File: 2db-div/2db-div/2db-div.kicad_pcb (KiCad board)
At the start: 2 copper layers, 63.5 x 43.2 mm, 26 parts, among them J1001 Conn_01x02, J1002 From R2, J1003 Conn_01x02, U1001 MC1458

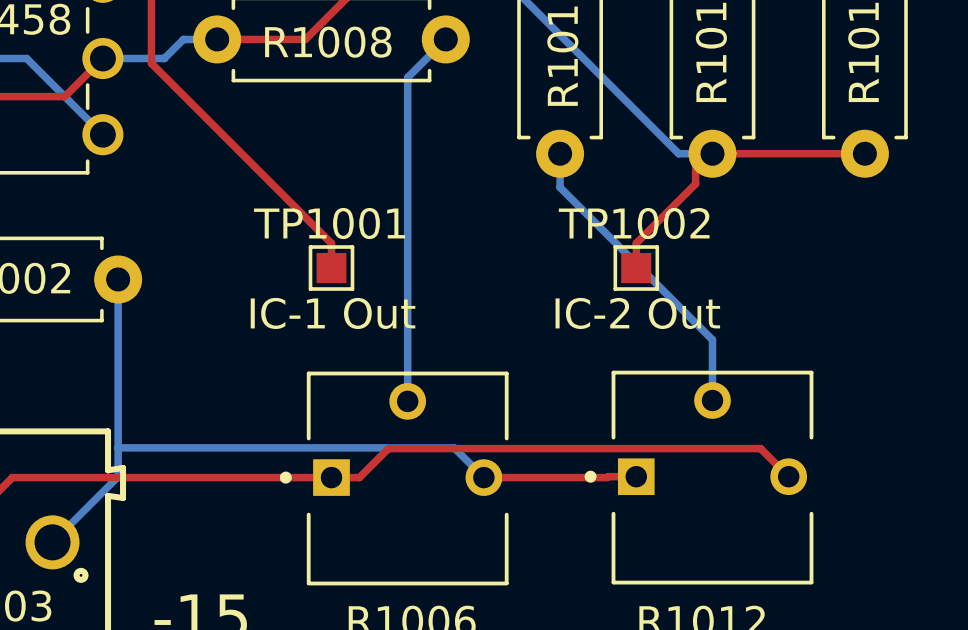
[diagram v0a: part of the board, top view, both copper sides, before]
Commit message: BOM for 2db-div
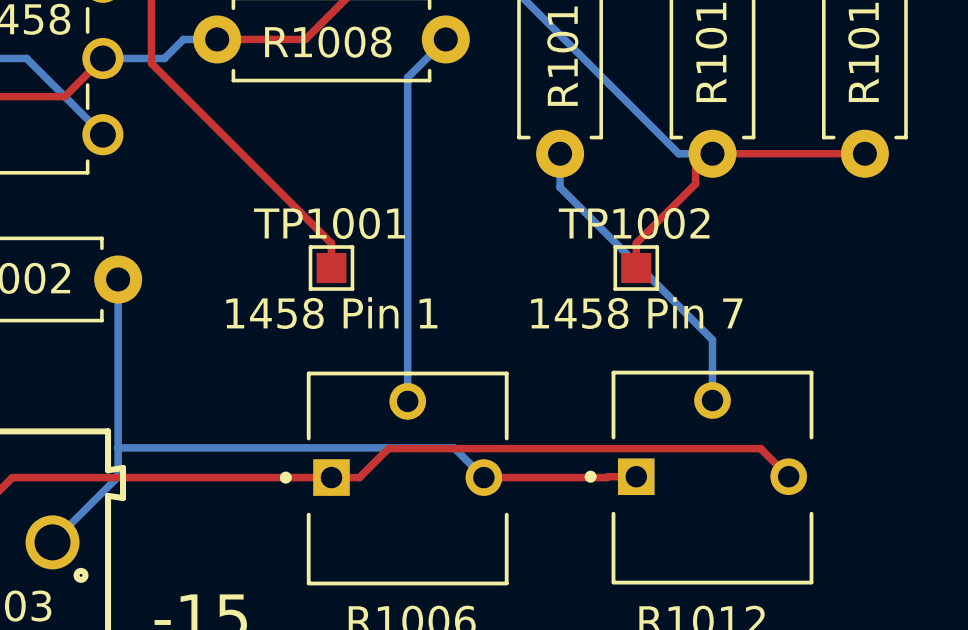
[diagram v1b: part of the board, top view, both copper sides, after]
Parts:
- D1001: value 1N4152 -> 1N4148
- TP1001: value IC-1 Out -> 1458 Pin 1
- TP1002: value IC-2 Out -> 1458 Pin 7
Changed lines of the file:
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@@
       (effects (font (size 1 1) (thickness 0.15)))
     )
-    (fp_text value "IC-2 Out" (at 0 1.55) (layer "F.SilkS")
+    (fp_text value "1458 Pin 7" (at 0 1.55) (layer "F.SilkS")
       (effects (font (size 1 1) (thickness 0.15)))
     )
@@
       (effects (font (size 0.75 0.75) (thickness 0.15)))
     )
-    (fp_text value "1N4152" (at 3.81 2.12) (layer "F.Fab")
+    (fp_text value "1N4148" (at 3.81 2.12) (layer "F.Fab")
       (effects (font (size 1 1) (thickness 0.15)))
     )
@@
       (effects (font (size 1 1) (thickness 0.15)))
     )
-    (fp_text value "IC-1 Out" (at 0 1.55) (layer "F.SilkS")
-      (effects (font (size 1 1) (thickness 0.15)))
-    )
+    (fp_text value "1458 Pin 1" (at 0 1.55) (layer "F.SilkS")
+      (effects (font (size 1 1) (thickness 0.15)))
+    )

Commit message: vco-1stmixer bom
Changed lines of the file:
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@@
   )
   (setup
+    (stackup
+      (layer "F.SilkS" (type "Top Silk Screen"))
+      (layer "F.Paste" (type "Top Solder Paste"))
+      (layer "F.Mask" (type "Top Solder Mask") (thickness 0.01))
+      (layer "F.Cu" (type "copper") (thickness 0.035))
+      (layer "dielectric 1" (type "core") (thickness 1.51) (material "FR4") (epsilon_r 4.5) (loss_tangent 0.02))
+      (layer "B.Cu" (type "copper") (thickness 0.035))
+      (layer "B.Mask" (type "Bottom Solder Mask") (thickness 0.01))
+      (layer "B.Paste" (type "Bottom Solder Paste"))
+      (layer "B.SilkS" (type "Bottom Silk Screen"))
+      (copper_finish "None")
+      (dielectric_constraints no)
+    )
     (pad_to_mask_clearance 0)
     (grid_origin 142.24 139.7)
@@
     (property "Spice_Primitive" "D")
     (attr through_hole)
-    (fp_text reference "D1001" (at 4.191 0) (layer "F.SilkS")
-      (effects (font (size 0.75 0.75) (thickness 0.15)))
+    (fp_text reference "D1001" (at 4.318 0) (layer "F.SilkS")
+      (effects (font (size 0.5 0.5) (thickness 0.125)))
     )
     (fp_text value "1N4148" (at 3.81 2.12) (layer "F.Fab")
@@
       (effects (font (size 1 1) (thickness 0.15)))
     )
-    (fp_text user "*" (at -7.62 -9.0678) (layer "F.SilkS")
-      (effects (font (size 1 1) (thickness 0.15)))
-    )
-    (fp_text user "*" (at -7.62 -9.0678) (layer "F.SilkS")
-      (effects (font (size 1 1) (thickness 0.15)))
-    )
+    (fp_text user "*" (at -8.636 -9.398) (layer "F.SilkS")
+      (effects (font (size 1 1) (thickness 0.15)))
+    )
+    (fp_text user "*" (at -7.874 -9.398) (layer "F.SilkS")
+      (effects (font (size 1 1) (thickness 0.15)))
+    )

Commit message: Minor updates to 2nd db board
primarily renaming nets
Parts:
- H1001, H1002, H1003, H1004: value MountingHole -> type="R" model="MountingHole" lib=""

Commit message: updates to 2db board
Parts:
- added SW1001: 2dB, Connector_Wire:SolderWire-0.5sqmm_1x02_P4.6mm_D0.9mm_OD2.1mm, F.Cu at (197.8, 121.6)
- added SW1002: type="R" model="Video" lib="", Connector_Wire:SolderWire-0.5sqmm_1x02_P4.6mm_D0.9mm_OD2.1mm, F.Cu at (197.8, 125.7)
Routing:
- net Net-(SW1001-A): track 0.00 -> 14.9 mm
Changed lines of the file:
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@@
   (net 12 "Net-(R1009-Pad2)")
   (net 13 "Net-(R1010-Pad2)")
-  (net 14 "Net-(R1013-Pad2)")
+  (net 14 "Net-(SW1001-A)")
+  (net 15 "/Out")
+  (net 16 "Net-(SW1002-Pad1)")
+  (net 17 "unconnected-(SW1002-Pad2)")
   (footprint "MountingHole:MountingHole_3.2mm_M3" (layer "F.Cu")
     (at 199.771 101.6)
@@
     (pad "" np_thru_hole circle (at 0 0) (size 3.2 3.2) (drill 3.2) (layers "*.Cu" "*.Mask"))
   )
+  (footprint "Connector_Wire:SolderWire-0.5sqmm_1x02_P4.6mm_D0.9mm_OD2.1mm" (layer "F.Cu")
+    (at 197.838 121.58)
+    (descr "Soldered wire connection, for 2 times 0.5 mm² wires, basic insulation, conductor diameter 0.9mm, outer diameter 2.1mm, size source Multi-Contact FLEXI-E 0.5 (https://ec.staubli.com/AcroFiles/Catalogues/TM_Cab-Main-11014119_(en)_hi.pdf), bend radius 3 times outer diameter, generated with kicad-footprint-generator")
+    (tags "connector wire 0.5sqmm")
+    (property "Sheetfile" "2db-div.kicad_sch")
+    (property "Sheetname" "")
+    (property "Sim.Device" "SPICE")
+    (property "Sim.Enable" "0")
+    (property "Sim.Params" "type=\"R\" model=\"2dB\" lib=\"\"")
+    (property "Sim.Pins" "1=1 2=2 3=3")
+    (property "ki_description" "Switch, single pole double throw")
+    (property "ki_keywords" "switch single-pole double-throw spdt ON-ON")
+    (attr exclude_from_pos_files)
+    (fp_text reference "SW1001" (at 2.3 -2.25) (layer "F.SilkS")
+        (effects (font (size 1 1) (thickness 0.15)))
+    )
+    (fp_text value "2dB" (at 2.3 2.25) (layer "F.Fab")
+        (effects (font (size 1 1) (thickness 0.15)))
+    )
+    (fp_text user "${REFERENCE}" (at 2.3 0 90) (layer "F.Fab")
+        (effects (font (size 0.78 0.78) (thickness 0.12)))
+    )
+    (fp_line (start -1.8 -1.55) (end -1.8 1.55)
+      (stroke (width 0.05) (type solid)) (layer "F.CrtYd"))
+    (fp_line (start -1.8 1.55) (end 1.8 1.55)
+      (stroke (width 0.05) (type solid)) (layer "F.CrtYd"))
+    (fp_line (start 1.8 -1.55) (end -1.8 -1.55)
+      (stroke (width 0.05) (type solid)) (layer "F.CrtYd"))
+    (fp_line (start 1.8 1.55) (end 1.8 -1.55)
+      (stroke (width 0.05) (type solid)) (layer "F.CrtYd"))
+    (fp_line (start 2.8 -1.55) (end 2.8 1.55)
+      (stroke (width 0.05) (type solid)) (layer "F.CrtYd"))
+    (fp_line (start 2.8 1.55) (end 6.4 1.55)
+      (stroke (width 0.05) (type solid)) (layer "F.CrtYd"))
+    (fp_line (start 6.4 -1.55) (end 2.8 -1.55)
+      (stroke (width 0.05) (type solid)) (layer "F.CrtYd"))
+    (fp_line (start 6.4 1.55) (end 6.4 -1.55)
+      (stroke (width 0.05) (type solid)) (layer "F.CrtYd"))
+    (fp_circle (center 0 0) (end 1.05 0)
+      (stroke (width 0.1) (type solid)) (fill none) (layer "F.Fab"))
+    (fp_circle (center 4.6 0) (end 5.65 0)
+      (stroke (width 0.1) (type solid)) (fill none) (layer "F.Fab"))
+    (pad "1" thru_hole roundrect (at 0 0) (size 2.1 2.1) (drill 1.1) (layers "*.Cu" "*.Mask") (roundrect_rratio 0.119048)
+      (net 14 "Net-(SW1001-A)") (pinfunction "A") (pintype "passive"))
+    (pad "2" thru_hole circle (at 4.6 0) (size 2.1 2.1) (drill 1.1) (layers "*.Cu" "*.Mask")
+      (net 15 "/Out") (pinfunction "B") (pintype "passive"))
+    (model "${KICAD6_3DMODEL_DIR}/Connector_Wire.3dshapes/SolderWire-0.5sqmm_1x02_P4.6mm_D0.9mm_OD2.1mm.wrl"
+      (offset (xyz 0 0 0))
+      (scale (xyz 1 1 1))
+      (rotate (xyz 0 0 0))
+    )
+  )
   (footprint "Resistor_THT:R_Axial_DIN0207_L6.3mm_D2.5mm_P7.62mm_Horizontal" (layer "F.Cu")
     (at 181.61 111.379 180)
@@
     (pad "1" smd rect (at 0 0) (size 1 1) (layers "F.Cu" "F.Mask")
       (net 4 "Net-(D1001-K)") (pinfunction "1") (pintype "passive"))
+  )
+  (footprint "Connector_Wire:SolderWire-0.5sqmm_1x02_P4.6mm_D0.9mm_OD2.1mm" (layer "F.Cu")
+    (at 197.838 125.73)
+    (descr "Soldered wire connection, for 2 times 0.5 mm² wires, basic insulation, conductor diameter 0.9mm, outer diameter 2.1mm, size source Multi-Contact FLEXI-E 0.5 (https://ec.staubli.com/AcroFiles/Catalogues/TM_Cab-Main-11014119_(en)_hi.pdf), bend radius 3 times outer diameter, generated with kicad-footprint-generator")
+    (tags "connector wire 0.5sqmm")
+    (property "Sheetfile" "2db-div.kicad_sch")
+    (property "Sheetname" "")
+    (property "Sim.Device" "SPICE")
+    (property "Sim.Enable" "0")
+    (property "Sim.Params" "type=\"R\" model=\"Video\" lib=\"\"")
+    (property "Sim.Pins" "1=1 2=2 3=3 4=4")
+    (property "ki_description" "Switch, three position, single pole triple throw, 3 position switch, SP3T")
+    (property "ki_keywords" "switch sp3t ON-ON-ON")
+    (attr exclude_from_pos_files)
+    (fp_text reference "SW1002" (at 2.3 -2.25) (layer "F.SilkS")
+        (effects (font (size 1 1) (thickness 0.15)))
+    )
+    (fp_text value "type=\"R\" model=\"Video\" lib=\"\"" (at 2.3 2.25) (layer "F.Fab")
+        (effects (font (size 1 1) (thickness 0.15)))
+    )
+    (fp_text user "${REFERENCE}" (at 2.3 0 90) (layer "F.Fab")
+        (effects (font (size 0.78 0.78) (thickness 0.12)))
+    )
+    (fp_line (start -1.8 -1.55) (end -1.8 1.55)
+      (stroke (width 0.05) (type solid)) (layer "F.CrtYd"))
+    (fp_line (start -1.8 1.55) (end 1.8 1.55)
+      (stroke (width 0.05) (type solid)) (layer "F.CrtYd"))
+    (fp_line (start 1.8 -1.55) (end -1.8 -1.55)
+      (stroke (width 0.05) (type solid)) (layer "F.CrtYd"))
+    (fp_line (start 1.8 1.55) (end 1.8 -1.55)
+      (stroke (width 0.05) (type solid)) (layer "F.CrtYd"))
+    (fp_line (start 2.8 -1.55) (end 2.8 1.55)
+      (stroke (width 0.05) (type solid)) (layer "F.CrtYd"))
+    (fp_line (start 2.8 1.55) (end 6.4 1.55)
+      (stroke (width 0.05) (type solid)) (layer "F.CrtYd"))
+    (fp_line (start 6.4 -1.55) (end 2.8 -1.55)
+      (stroke (width 0.05) (type solid)) (layer "F.CrtYd"))
+    (fp_line (start 6.4 1.55) (end 6.4 -1.55)
+      (stroke (width 0.05) (type solid)) (layer "F.CrtYd"))
+    (fp_circle (center 0 0) (end 1.05 0)
+      (stroke (width 0.1) (type solid)) (fill none) (layer "F.Fab"))
+    (fp_circle (center 4.6 0) (end 5.65 0)
+      (stroke (width 0.1) (type solid)) (fill none) (layer "F.Fab"))
+    (pad "1" thru_hole roundrect (at 0 0) (size 2.1 2.1) (drill 1.1) (layers "*.Cu" "*.Mask") (roundrect_rratio 0.119048)
+      (net 16 "Net-(SW1002-Pad1)") (pinfunction "1") (pintype "passive"))
+    (pad "2" thru_hole circle (at 4.6 0) (size 2.1 2.1) (drill 1.1) (layers "*.Cu" "*.Mask")
+      (net 17 "unconnected-(SW1002-Pad2)") (pinfunction "2") (pintype "passive+no_connect"))
+    (model "${KICAD6_3DMODEL_DIR}/Connector_Wire.3dshapes/SolderWire-0.5sqmm_1x02_P4.6mm_D0.9mm_OD2.1mm.wrl"
+      (offset (xyz 0 0 0))
+      (scale (xyz 1 1 1))
+      (rotate (xyz 0 0 0))
+    )
   )
   (footprint "2db-div:TRIM_3362P-1-103LF" (layer "F.Cu")
@@
     (property "Sheetfile" "2db-div.kicad_sch")
     (property "Sheetname" "")
+    (property "Sim.Device" "SUBCKT")
     (property "Sim.Enable" "0")
     (property "Sim.Library" "2db-div-spice\\LM358-dual.lib")
@@
       (net 4 "Net-(D1001-K)") (pintype "passive"))
     (pad "2" thru_hole oval (at 7.62 0 90) (size 1.6 1.6) (drill 0.8) (layers "*.Cu" "*.Mask")
-      (net 14 "Net-(R1013-Pad2)") (pintype "passive"))
+      (net 14 "Net-(SW1001-A)") (pintype "passive"))
     (model "${KICAD6_3DMODEL_DIR}/Resistor_THT.3dshapes/R_Axial_DIN0207_L6.3mm_D2.5mm_P7.62mm_Horizontal.wrl"
       (offset (xyz 0 0 0))
@@
   (segment (start 185.42 116.3143) (end 190.5 121.3943) (width 0.25) (layer "B.Cu") (net 13))
   (segment (start 185.42 115.189) (end 185.42 116.3143) (width 0.25) (layer "B.Cu") (net 13))
+  (segment (start 195.58 107.569) (end 197.838 109.827) (width 0.25) (layer "F.Cu") (net 14))
+  (segment (start 197.838 109.827) (end 197.838 121.58) (width 0.25) (layer "F.Cu") (net 14))
   (zone (net 2) (net_name "GND") (layers "F&B.Cu") (hatch edge 0.508)
     (connect_pads (clearance 0.508))

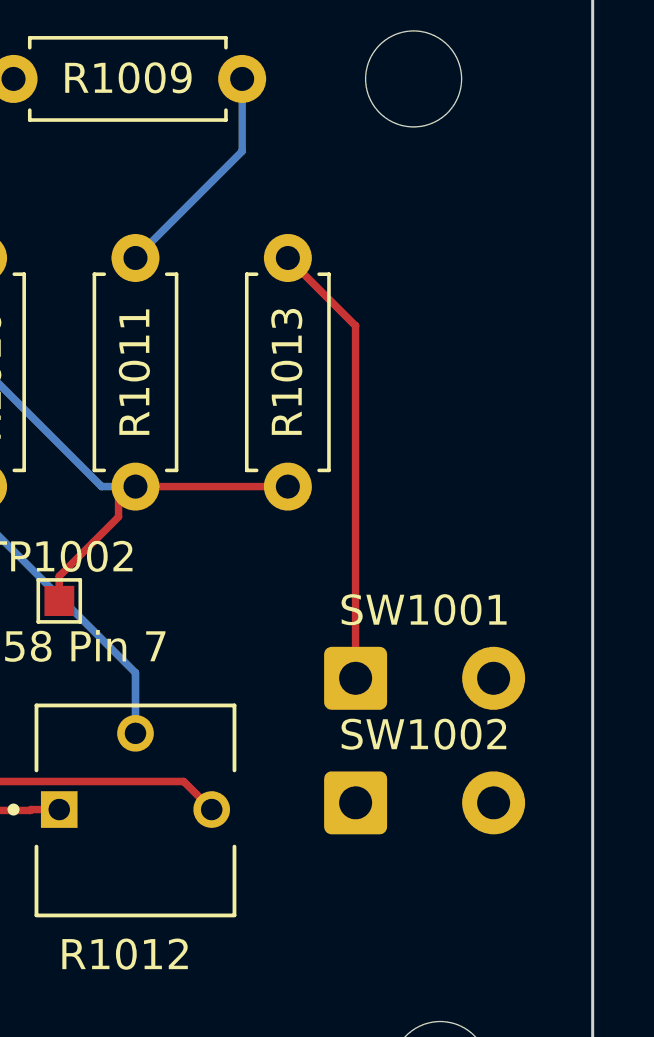
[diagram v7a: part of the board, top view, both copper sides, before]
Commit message: minor 2db/div changes
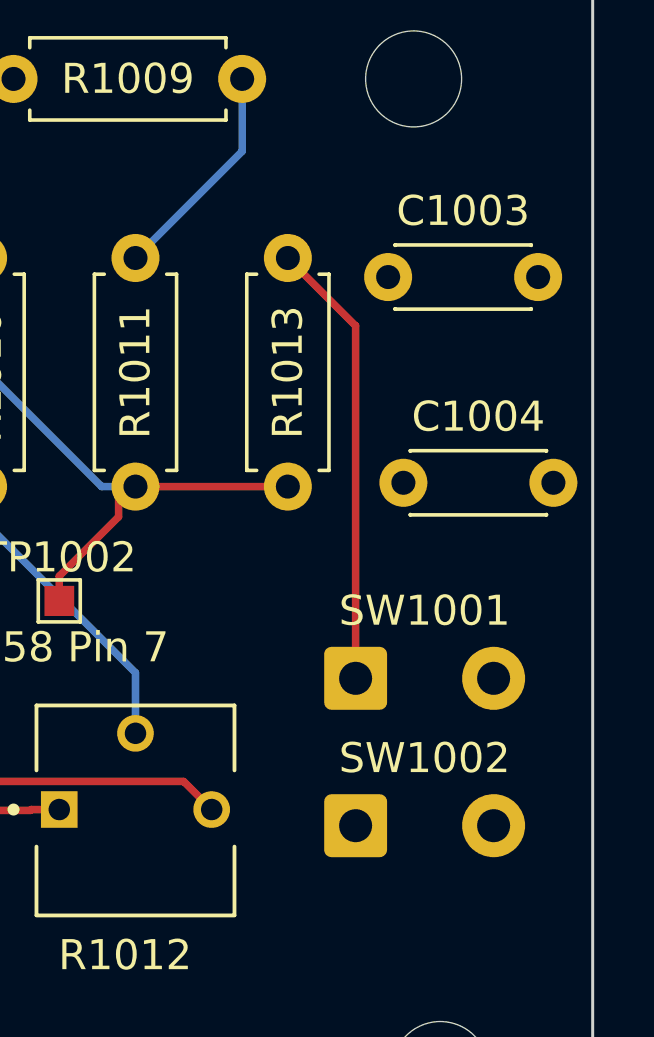
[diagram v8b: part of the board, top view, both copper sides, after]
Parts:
- added C1003: .1u, Capacitor_THT:C_Disc_D4.3mm_W1.9mm_P5.00mm, F.Cu at (198.9, 108.2)
- added C1004: 3.3u, Capacitor_THT:C_Disc_D4.3mm_W1.9mm_P5.00mm, F.Cu at (199.4, 115.1)
- moved SW1002 0.76 mm to (197.8, 126.5)
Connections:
- SW1002 pad 2: unconnected-(SW1002-Pad2) -> Net-(C1003-Pad1)
